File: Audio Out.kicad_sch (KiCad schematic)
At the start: 20 parts

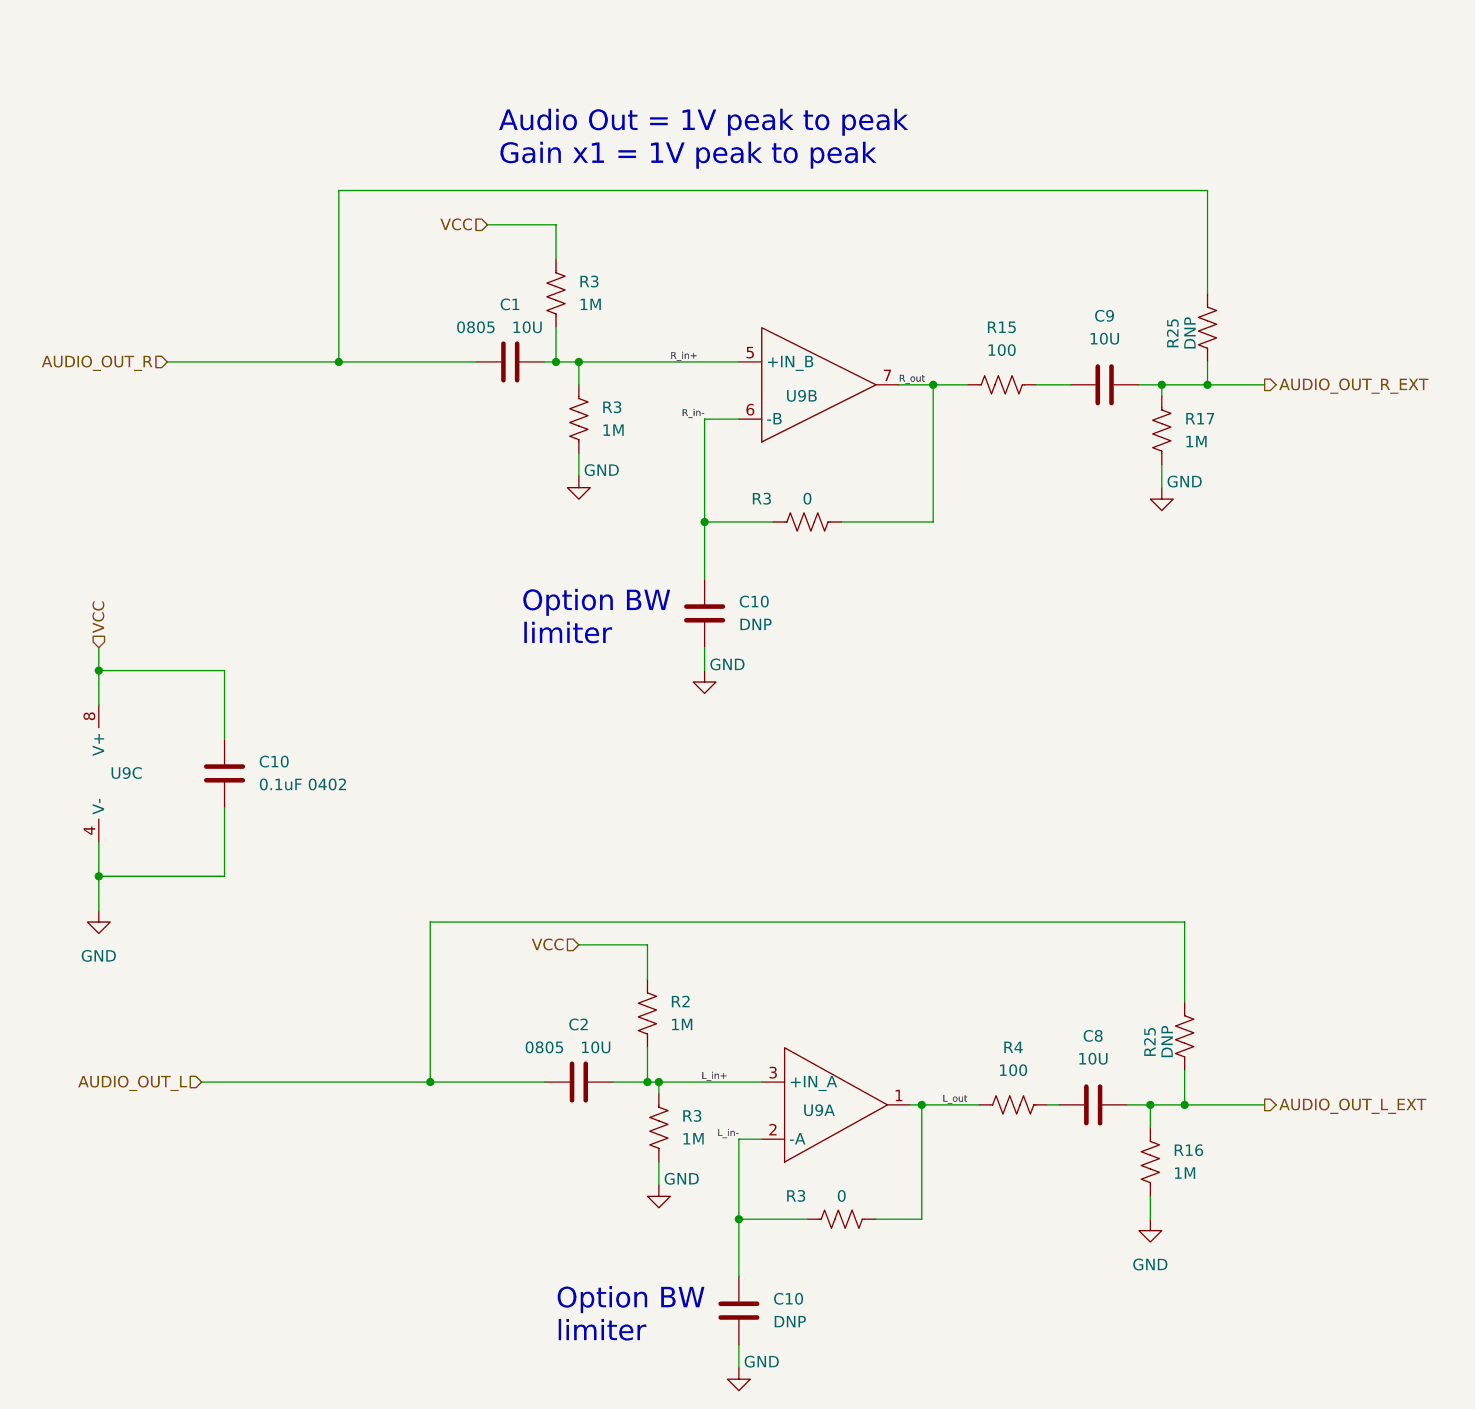
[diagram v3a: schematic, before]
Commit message: adding script to pull prices and availability from Mouser
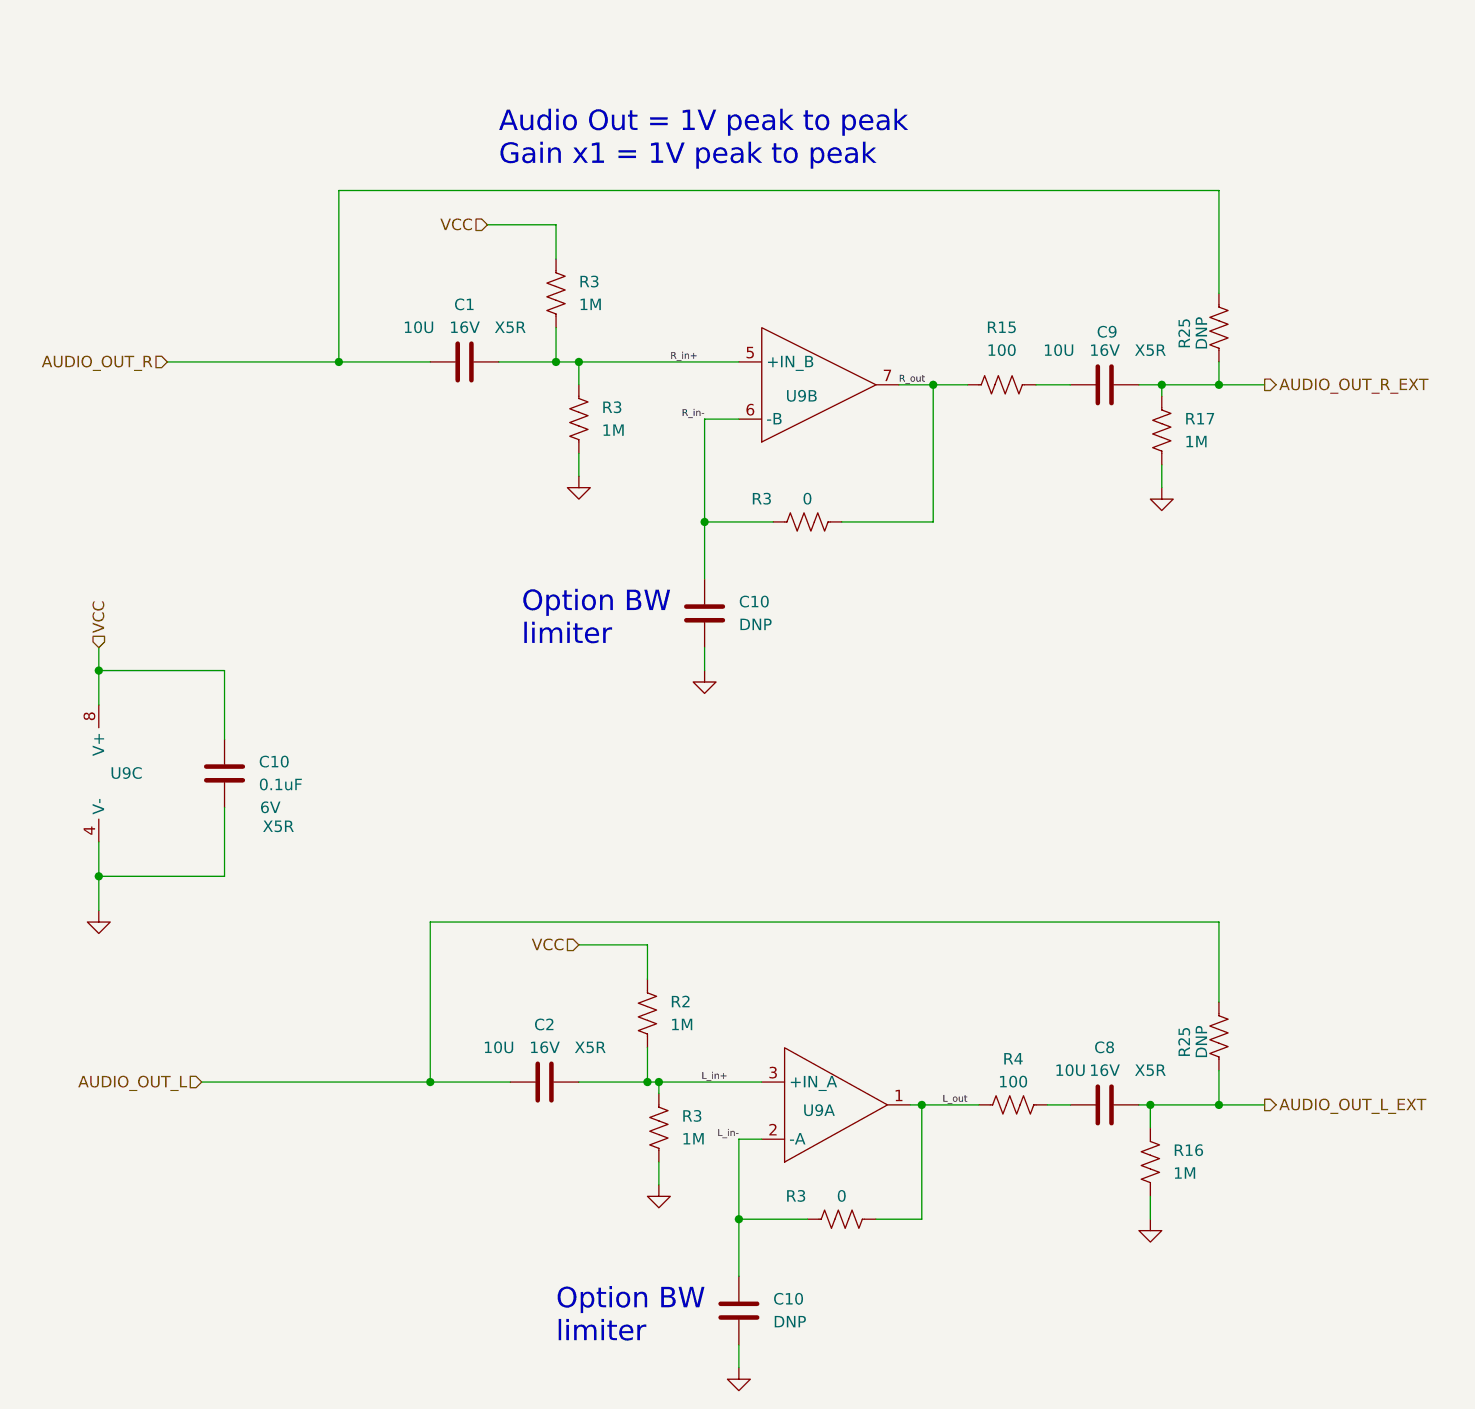
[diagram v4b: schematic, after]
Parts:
- C1, C2: Specs 0805 -> (none); Type (none) -> X5R; Voltage (none) -> 16V
- C10: value 0.1uF 0402 -> 0.1uF; Type (none) -> X5R; Voltage (none) -> 6V
- C8, C9: Type (none) -> X5R; Voltage (none) -> 16V
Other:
- moved on the sheet: C1, C2, C8, R25

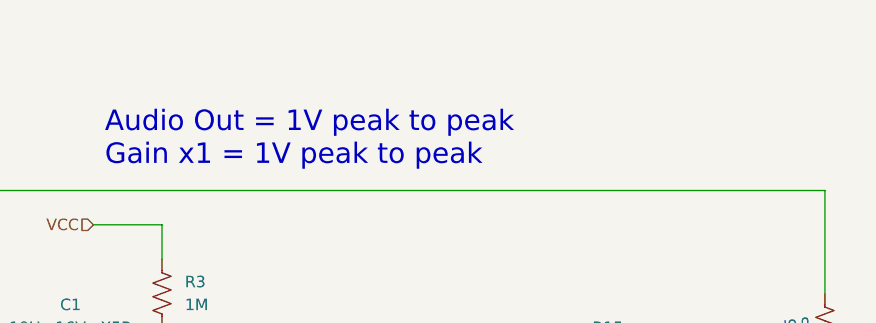
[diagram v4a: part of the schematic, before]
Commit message: script working to generate Mouser, Digikey, and JLPCB BOMS
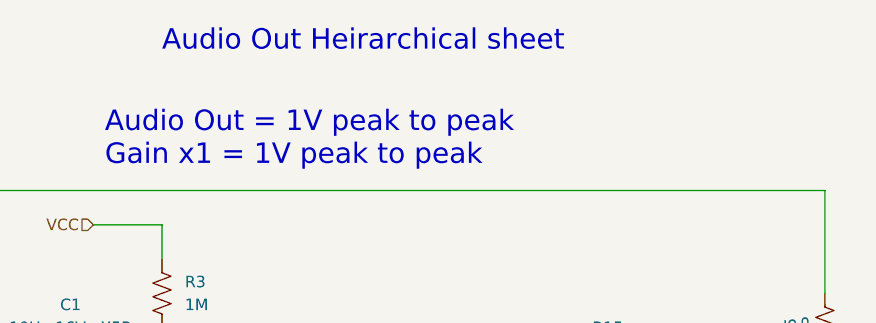
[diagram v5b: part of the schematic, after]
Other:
- note added: "Audio Out Heirarchical sheet"
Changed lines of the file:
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@@
+    (effects (font (size 2.27 2.27)) (justify left bottom))
+  )
+  (text "Audio Out Heirarchical sheet" (at 105.41 16.51 0)
     (effects (font (size 2.27 2.27)) (justify left bottom))
   )
